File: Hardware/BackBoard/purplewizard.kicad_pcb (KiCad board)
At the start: 2 copper layers, 92.5 x 151 mm, 165 parts, among them J1 3.3V, J10 SPKR-, J11 JTAG, J12 TagConnect, J13 Minibadge Expansion, J14 Battery, J15 USB_C_Receptacle_USB2.0, J16 Conn_01x50, J17 Board to Board, J18 Micro_SD_Card, J19 3.3V, J2 GND, J20 P1.06, J21 P1.05, J22 LCD_MISO, J23 LCD_RD, J24 LCD_TE, J25 MOUT, J26 MIC+, J27 GND, J28 UPDI, J29 GND, J3 UART_TX, J30 USB-, J31 USB+, J32 VBUS, J4 UART_RX, J5 LCD_SCK, J6 LCD_MOSI, J7 P1.07, J8 LCD_WR, J9 SPKR+, Q1 FDN360P, SW1 Power, SW10 TACTILE, SW11 TACTILE, SW12 TACTILE, SW13 TACTILE, SW14 TACTILE, SW15 TACTILE, SW16 TACTILE, SW17 TACTILE, SW18 SKRHABE010, SW19 SKRHABE010, SW2 TACTILE, SW3 TACTILE, SW4 TACTILE, SW5 TACTILE, SW6 TACTILE, SW7 TACTILE, SW8 TACTILE, SW9 TACTILE, U1 NAU8810, U2 PAM2305AABADJ, U3 BMD-340, U4 MCP73832-2-OT, U5 S25FL256S, U6 IS31FL3736, U7 ATtiny1617-M, X1 Badgelife_sao_connector_v169b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

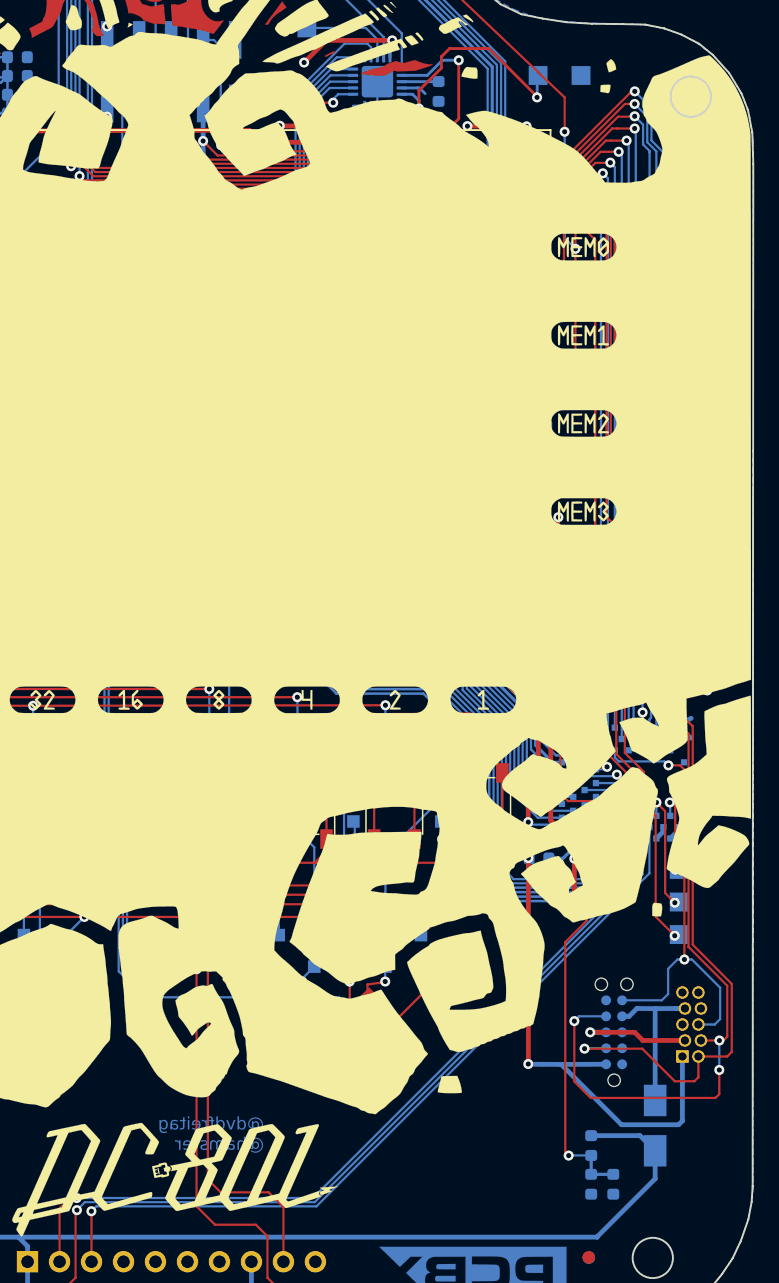
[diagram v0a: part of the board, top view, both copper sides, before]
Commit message: Adding PogoProto jig Fixed upper right hole being off 3/4 of a millimeter Added some pads for USB and added some vias to help pogo pin alignment
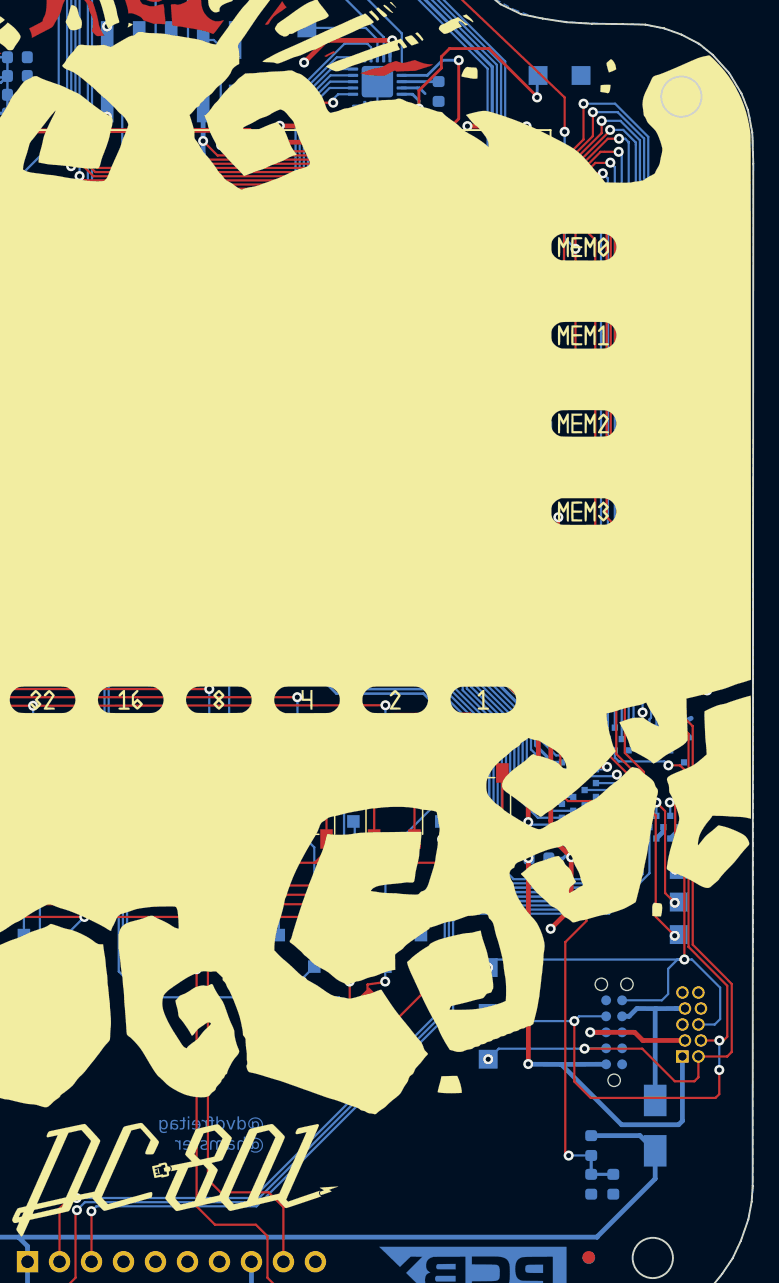
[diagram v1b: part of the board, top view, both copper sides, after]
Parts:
- added J33: SWDIO, TestPoint:TestPoint_Pad_1.5x1.5mm, B.Cu at (173.4, 150.0)
- added J34: SWCLK, TestPoint:TestPoint_Pad_1.5x1.5mm, B.Cu at (173.4, 146.4)
- added J35: SWO, TestPoint:TestPoint_Pad_1.5x1.5mm, B.Cu at (173.4, 142.8)
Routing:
- net SW0: track 37.2 -> 53.0 mm, vias 2 -> 3
- net SWDIO: track 47.5 -> 55.5 mm, vias 2 -> 3
- net SWCLK: track 56.7 -> 63.8 mm, vias 4 -> 5
- net MB_SCK: track 63.1 -> 67.2 mm
- net MB_MOSI: track 64.8 -> 68.9 mm
- net MB_MISO: track 66.0 -> 70.1 mm
- net GND: track 244.7 -> 246.4 mm
- net EXP1: track 101.4 -> 100.6 mm
- net SDA: track 288.5 -> 287.8 mm
- net EXP2: track 96.8 -> 96.2 mm
- net SCL: track 297.2 -> 296.6 mm
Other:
- outline, holes or cut-outs redrawn
- board text added: "SWCLK"
- board text added: "SWDIO"
- board text removed: "SWCLK GND"
- board text removed: "SWDIO 3v3"

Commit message: Final fab files for the PCBs
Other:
- rule pad_to_mask_clearance: 0.2 -> 0

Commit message: Uprev to 1.1 to support current parts availability Added solderpaste to USB connector through-pins
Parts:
- removed D4: SP0503BAHT, Package_TO_SOT_SMD:SOT-143
- removed R17: 540k, Resistor_SMD:R_0603_1608Metric
- removed R18: 120k, Resistor_SMD:R_0603_1608Metric
- D24, D25, D26, D27, D28, D29, D30, D31, D32, D33, D34, D35, D36, D37, D38, D39, D40, D41, D42, D43, D44, D45, D46, D47, D48, D49: footprint Diode_SMD:D_SOD-323_HandSoldering -> Diode_SMD:D_SOD-523
- L1: value 4.7uH -> 1uH; footprint Inductor_SMD:L_0805_2012Metric -> Inductor_SMD:L_1008_2520Metric
- Q1: value FDN360P -> AO3409
- U2: value PAM2305AABADJ -> SC189ZULTRT; footprint Package_TO_SOT_SMD:SOT-23-5 -> lib_fp:SC189ZULTRT
- moved L1 3.86 mm to (106.6, 155.4)
- moved C6 2.71 mm to (109.1, 152.4), turned to 0 degrees
- moved U2 1.73 mm to (109.4, 155.1), turned to -90 degrees
- moved C3 1.63 mm to (109.5, 157.2), turned to 180 degrees
- moved REF** 0.34 mm to (148.2, 98.5)
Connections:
- J11 pad 10: Net-(J11-Pad10) -> unconnected-(J11-Pad10)
- J11 pad 5: Net-(J11-Pad5) -> unconnected-(J11-Pad5)
- J11 pad 8: Net-(J11-Pad8) -> unconnected-(J11-Pad8)
- J11 pad 9: Net-(J11-Pad9) -> unconnected-(J11-Pad9)
- J12 pad 10: Net-(J12-Pad10) -> unconnected-(J12-Pad10)
- J12 pad 5: Net-(J12-Pad5) -> unconnected-(J12-Pad5)
- J12 pad 8: Net-(J12-Pad8) -> unconnected-(J12-Pad8)
- J12 pad 9: Net-(J12-Pad9) -> unconnected-(J12-Pad9)
- J13 pad 10: Net-(J13-Pad10) -> unconnected-(J13-Pad10)
- J13 pad 11: Net-(J13-Pad11) -> unconnected-(J13-Pad11)
- J13 pad 12: Net-(J13-Pad12) -> unconnected-(J13-Pad12)
- J13 pad 13: Net-(J13-Pad13) -> unconnected-(J13-Pad13)
- J13 pad 14: Net-(J13-Pad14) -> unconnected-(J13-Pad14)
- J13 pad 6: Net-(J13-Pad6) -> unconnected-(J13-Pad6)
- J13 pad 7: Net-(J13-Pad7) -> unconnected-(J13-Pad7)
- J13 pad 8: Net-(J13-Pad8) -> unconnected-(J13-Pad8)
- J13 pad 9: Net-(J13-Pad9) -> unconnected-(J13-Pad9)
- J15 pad A8: Net-(J15-PadA8) -> unconnected-(J15-PadA8)
- J15 pad B8: Net-(J15-PadB8) -> unconnected-(J15-PadB8)
- J18 pad 1: Net-(J18-Pad1) -> unconnected-(J18-Pad1)
- J18 pad 12: Net-(J18-Pad12) -> unconnected-(J18-Pad12)
- J18 pad 13: Net-(J18-Pad13) -> unconnected-(J18-Pad13)
- J18 pad 14: Net-(J18-Pad14) -> unconnected-(J18-Pad14)
- J18 pad 8: Net-(J18-Pad8) -> unconnected-(J18-Pad8)
- SW1 pad 1: Net-(SW1-Pad1) -> unconnected-(SW1-Pad1)
- U1 pad 1: Net-(U1-Pad1) -> unconnected-(U1-Pad1)
- U1 pad 19: Net-(U1-Pad19) -> unconnected-(U1-Pad19)
- U2 pad 1: +BATT_SW -> (no net)
- U2 pad 2: GND -> +BATT_SW
- U2 pad 4: Net-(R17-Pad1) -> Net-(L1-Pad1)
- U2 pad 5: Net-(L1-Pad1) -> GND
- U3 pad 13: Net-(U3-Pad13) -> unconnected-(U3-Pad13)
- U3 pad 51: Net-(U3-Pad51) -> unconnected-(U3-Pad51)
- U3 pad 52: Net-(U3-Pad52) -> unconnected-(U3-Pad52)
- U3 pad 57: Net-(U3-Pad57) -> unconnected-(U3-Pad57)
- U3 pad 58: Net-(U3-Pad58) -> unconnected-(U3-Pad58)
- U3 pad 59: Net-(U3-Pad59) -> unconnected-(U3-Pad59)
- U3 pad 60: Net-(U3-Pad60) -> unconnected-(U3-Pad60)
- U6 pad 1: Net-(U6-Pad1) -> unconnected-(U6-Pad1)
- U6 pad 10: Net-(U6-Pad10) -> unconnected-(U6-Pad10)
- U6 pad 12: Net-(U6-Pad12) -> unconnected-(U6-Pad12)
- U6 pad 13: Net-(U6-Pad13) -> unconnected-(U6-Pad13)
- U6 pad 14: Net-(U6-Pad14) -> unconnected-(U6-Pad14)
- U6 pad 2: Net-(U6-Pad2) -> unconnected-(U6-Pad2)
- U6 pad 21: Net-(U6-Pad21) -> unconnected-(U6-Pad21)
- U6 pad 22: Net-(U6-Pad22) -> unconnected-(U6-Pad22)
- U6 pad 24: Net-(U6-Pad24) -> unconnected-(U6-Pad24)
- U6 pad 25: Net-(U6-Pad25) -> unconnected-(U6-Pad25)
- U6 pad 3: Net-(U6-Pad3) -> unconnected-(U6-Pad3)
- U6 pad 32: Net-(U6-Pad32) -> unconnected-(U6-Pad32)
- U6 pad 37: Net-(U6-Pad37) -> unconnected-(U6-Pad37)
- U7 pad 21: Net-(U7-Pad21) -> unconnected-(U7-Pad21)
- U7 pad 7: Net-(U7-Pad7) -> unconnected-(U7-Pad7)
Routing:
- net Net-(C10-Pad2): track 20.2 -> 14.7 mm
- net Net-(C11-Pad1): track 14.9 -> 9.57 mm
- net Net-(R17-Pad1): track 3.50 -> 0.00 mm
- net +3V3: track 614.5 -> 611.4 mm, vias 26 -> 25
- net unconnected-(U3-Pad13): track 0.00 -> 2.68 mm
- net Net-(U3-Pad13): track 2.68 -> 0.00 mm
- net +BATT_SW: track 116.1 -> 113.9 mm
- net unconnected-(U1-Pad19): track 0.00 -> 2.04 mm
- net Net-(U1-Pad19): track 2.04 -> 0.00 mm
- net unconnected-(U1-Pad1): track 0.00 -> 1.71 mm
- net Net-(U1-Pad1): track 1.71 -> 0.00 mm
- net unconnected-(U7-Pad7): track 0.00 -> 1.64 mm
- net Net-(U7-Pad7): track 1.64 -> 0.00 mm
- net GND: track 246.4 -> 248.0 mm, vias 59 -> 57
- net unconnected-(U7-Pad21): track 0.00 -> 1.00 mm
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- removed copper zone on B.Cu, net +BATT_SW
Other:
- board size 92.5 x 151 mm -> 92.5 x 150.6 mm
- net class Default removed
- board text added: "HP"
- board text added: "Rev 1.1"
- board text added: "SPKR"
- board text removed: "Rev 1"
- board text removed: "SPKR HP"
